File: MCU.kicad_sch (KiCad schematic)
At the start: 38 parts, among them Q1 BSS138, SW1 SW_Push, U1 STM32F722RETx, Y1 CSTNE8M00G55Z000R0

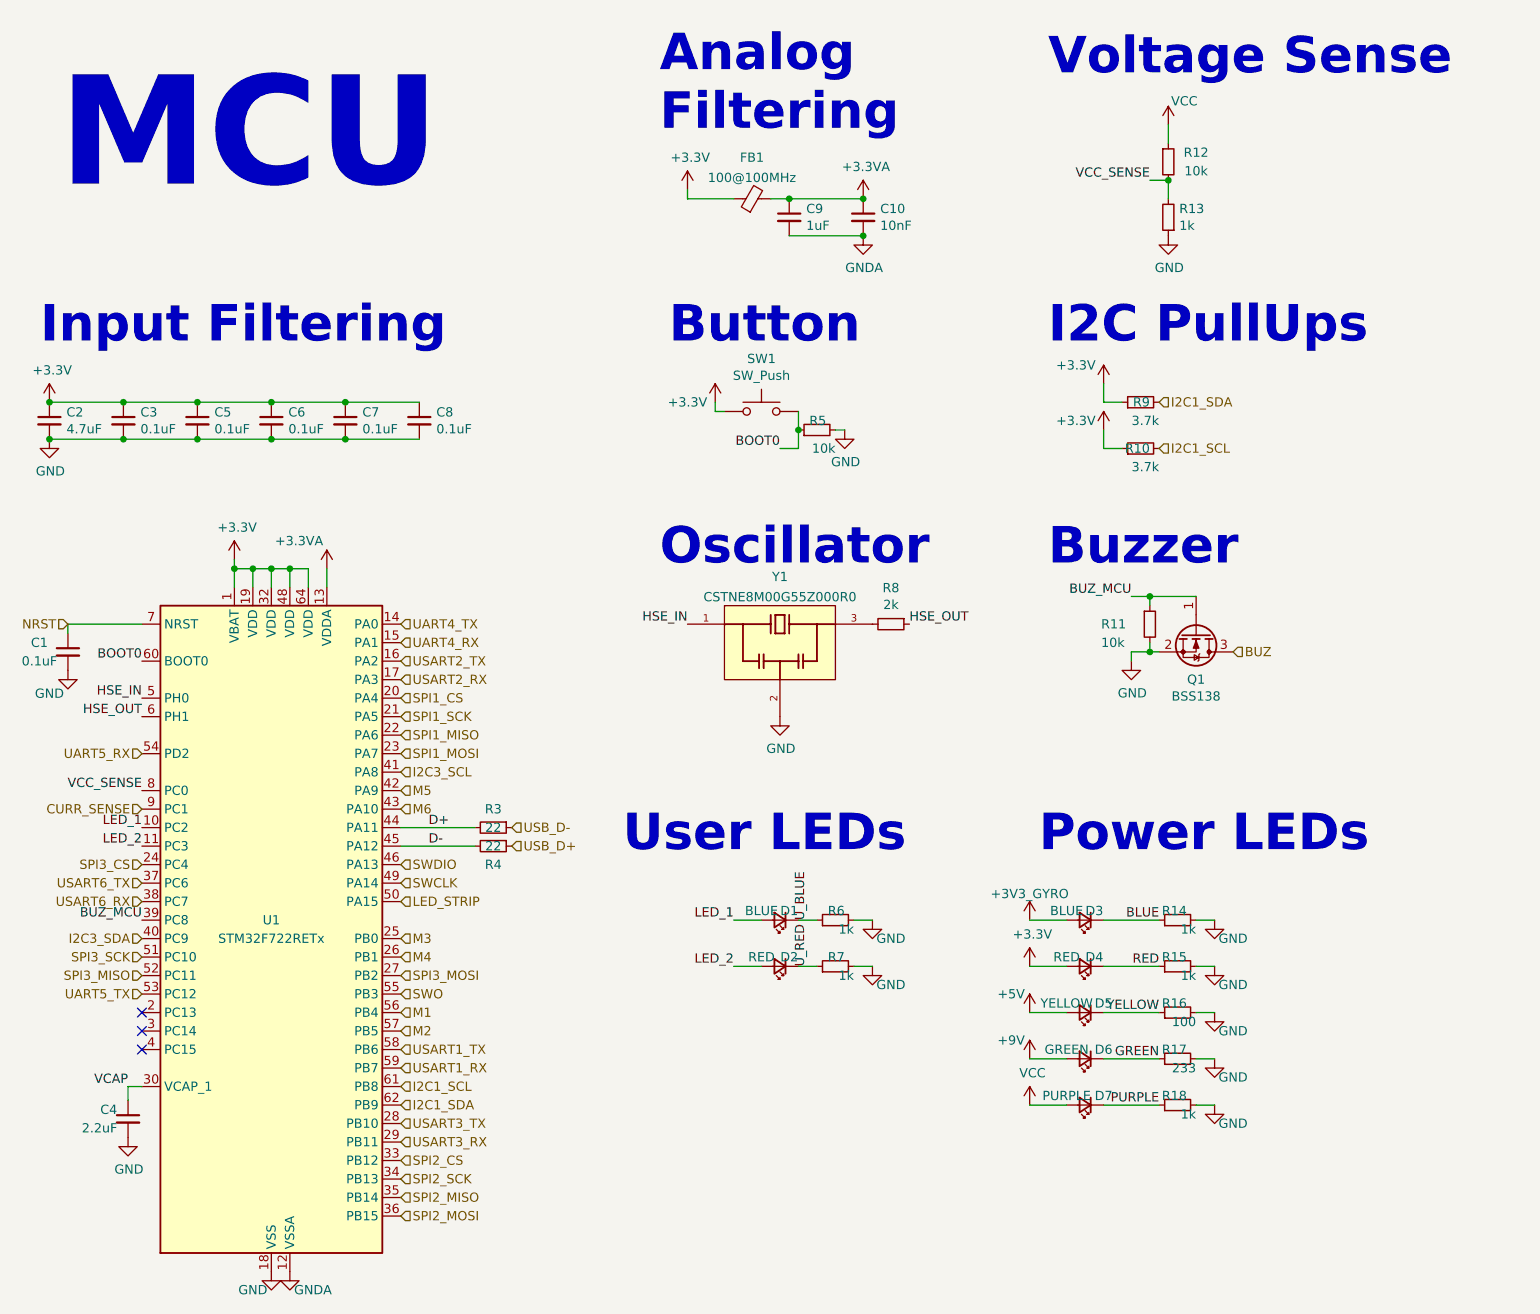
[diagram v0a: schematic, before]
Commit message: Finished power and signal routing.
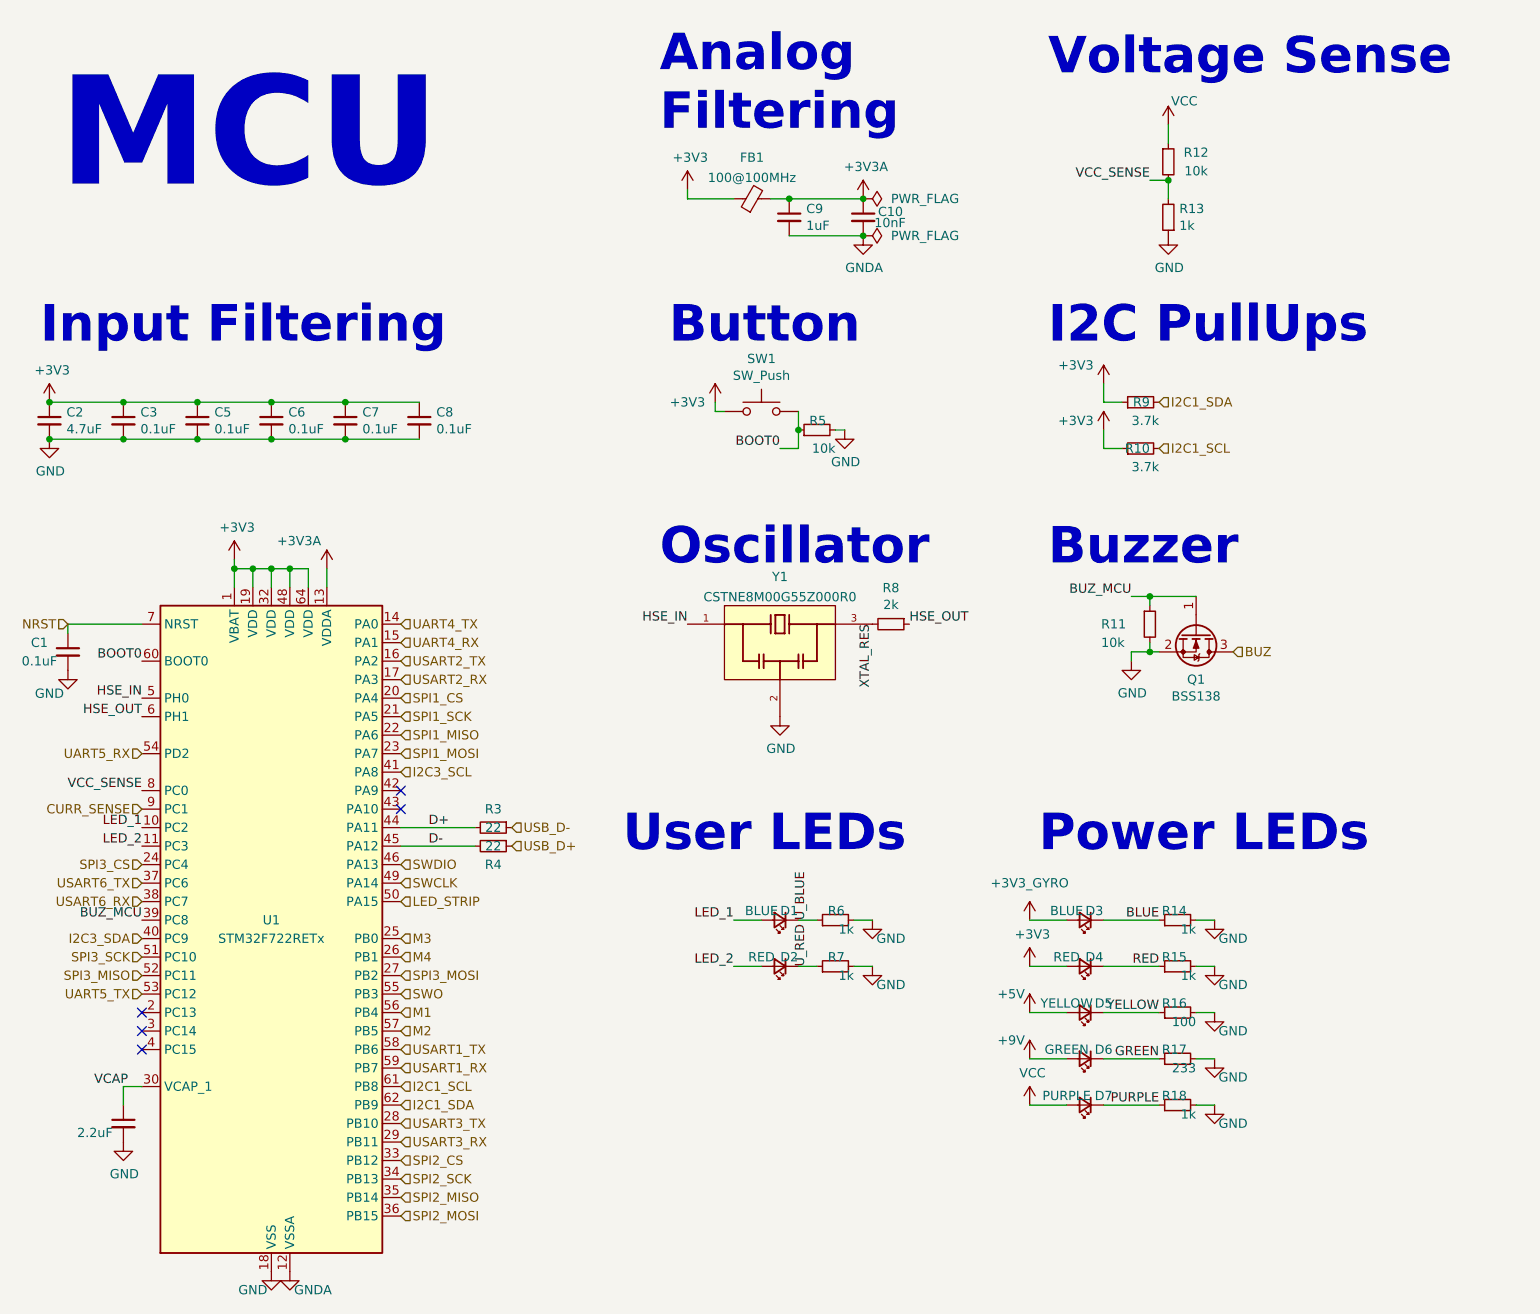
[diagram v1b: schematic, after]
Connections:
- net XTAL_RES: now reaches R8.2, Y1.3
- net +3.3V renamed +3V3
- net +3.3VA renamed +3V3A
- net M5: no longer names the net of U1.42 (PA9)
- net M6: no longer names the net of U1.43 (PA10)
- no-connect marks 3 -> 5
